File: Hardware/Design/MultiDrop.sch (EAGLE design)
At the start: 12 parts

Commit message: Hardware: evaluation pwr mgt with RPUpi ^1 shield
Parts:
- removed PM2: (no value), Documentation:TRUSTWORTHY
- removed U$5: BUS_MGR, Documentation:BUS_MGR
- added PM1: (no value), Documentation:DESKTOP
- added U$3: BUS_MGR, Documentation:BUS_MGR
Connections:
- net +DTR: now also U$3.+DTR; no longer U$1.+DTR
- net +DTR3: now also U$1.+DTR; no longer U$5.+DTR
- net +RX: now also U$3.+RX; no longer U$1.+RX
- net +RX3: now also U$1.+RX; no longer U$5.+RX
- net +TX: now also U$3.+TX; no longer U$1.+TX
- net +TX3: now also U$1.+TX; no longer U$5.+TX
- net -DTR: now also U$3.-DTR; no longer U$1.-DTR
- net -DTR3: now also U$1.-DTR; no longer U$5.-DTR
- net -RX: now also U$3.-RX; no longer U$1.-RX
- net -RX3: now also U$1.-RX; no longer U$5.-RX
- net -TX: now also U$3.-TX; no longer U$1.-TX
- net -TX3: now also U$1.-TX; no longer U$5.-TX
- net N$1: now also U$3.BM_TX; no longer U$1.BM_TX
- net N$14: now also U$1.BM_TX; no longer U$5.BM_TX
- net N$2: now also U$3.BM_RX; no longer U$1.BM_RX
- net N$21: now also U$1.BM_RX; no longer U$5.BM_RX
- net N$29: now also U$3.PWR; no longer U$1.PWR
- net N$3: now also PM1.TX; no longer PM2.TX
- net N$30: now also BM2.!RESET, U$3.DIO10; no longer BM2.RESET, U$1.DIO
- net N$32: now also U$1.I2C; no longer U$5.I2C
- net N$33: now also U$3.I2C; no longer U$1.I2C
- net N$4: now also U$3.!CTS; no longer U$1.!CTS
- net N$41: now also BM3.SHLD_5V, U$1.PWR; no longer BM3.SHLD_VIN, U$5.PWR
- net N$43: now also BM3.!RESET, U$1.DIO10; no longer BM3.RESET, U$5.DIO
- net N$44: now also BM1.!RESET, U$2.DIO10; no longer BM1.RESET, U$2.DIO
- net N$45: now also BM1.SHLD_5V; no longer BM1.SHLD_VIN
- net N$5: now also U$3.!RTS; no longer U$1.!RTS
- net N$6: now also U$3.!DTR; no longer U$1.!DTR
- net N$7: now also U$3.!DSR; no longer U$1.!DSR
- net N$8: now also U$3.HOST_RX; no longer U$1.PM_RX
- net N$9: now also U$3.HOST_TX; no longer U$1.PM_TX

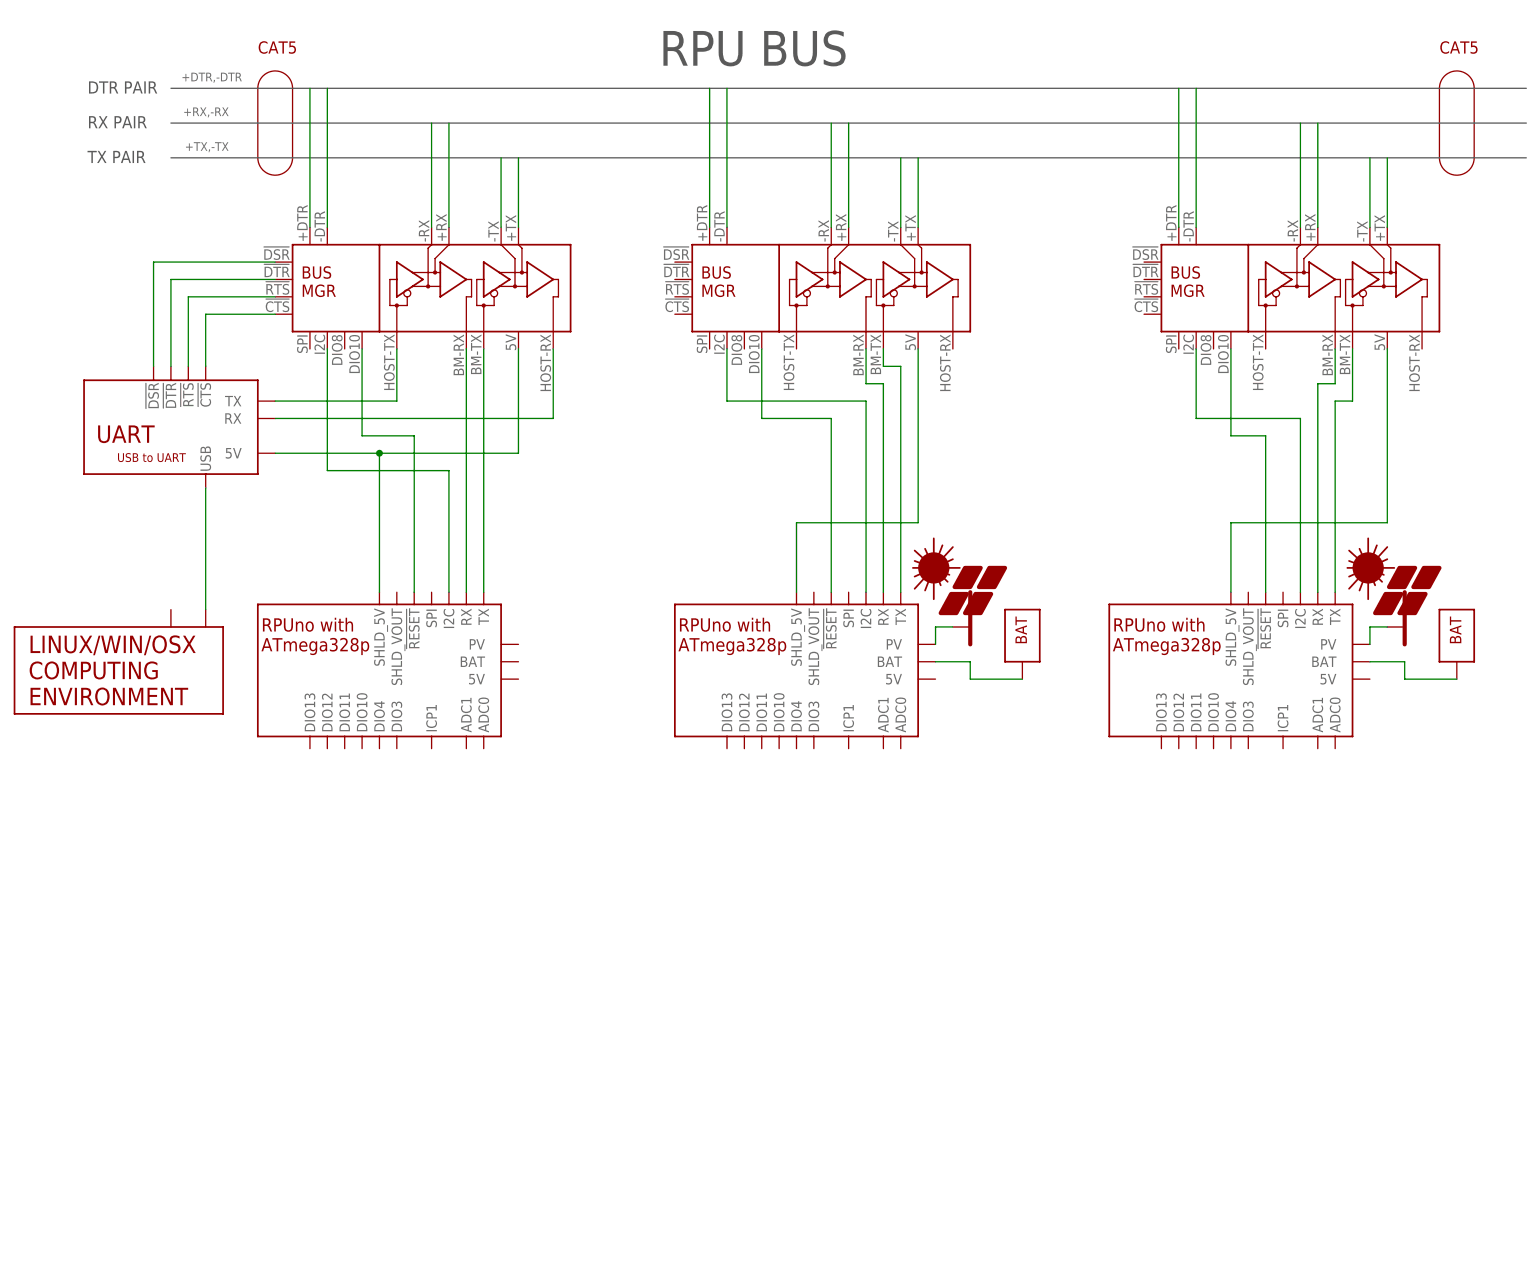
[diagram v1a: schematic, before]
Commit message: Hardware: ^7 review, removed LT3652
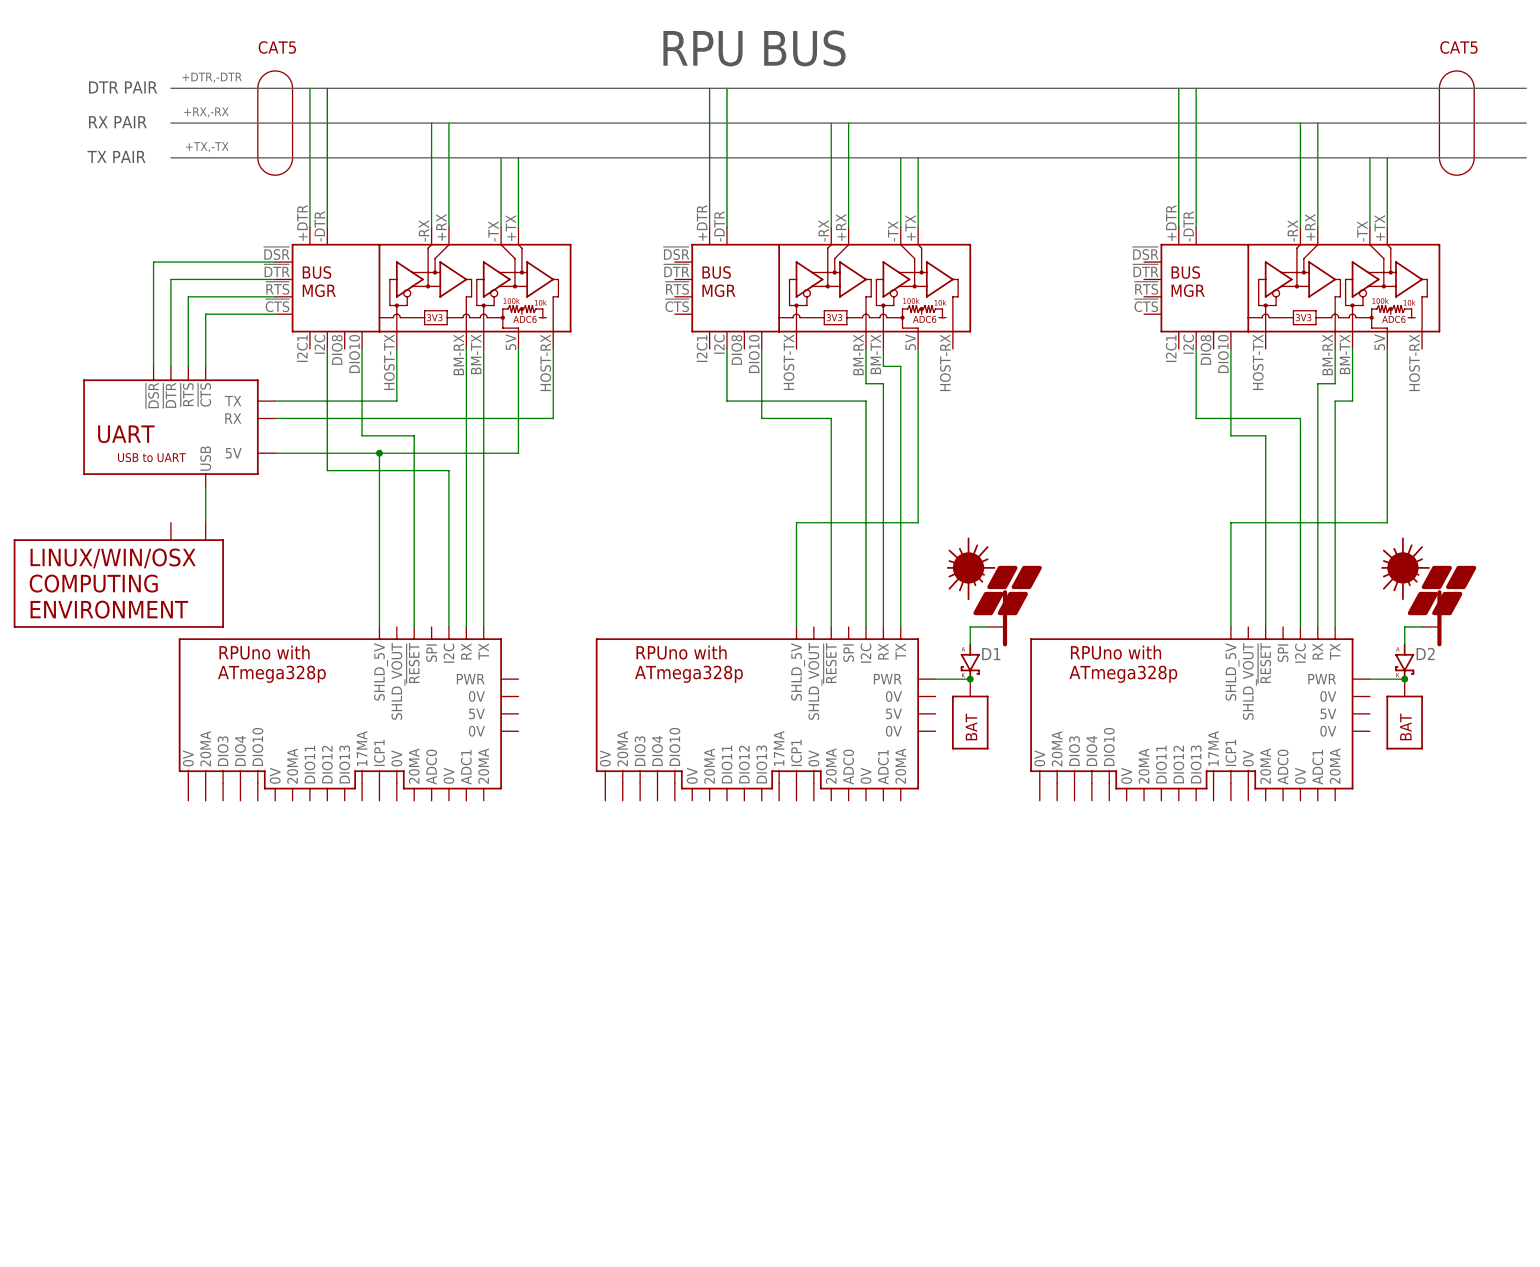
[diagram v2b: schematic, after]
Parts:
- added D1, D2: (no value), D-SBR:DSMC
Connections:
- removed net N$17: BM1.BAT, U$9.BAT_PWR
- removed net N$31: BM3.BAT, U$7.BAT_PWR
- removed net N$34: BM3.PV, PV4.PV_PWR
- removed net N$36: BM1.PV, PV2.PV_PWR
- new net N$12: BM3.PWR, D2.K, U$7.BAT_PWR
- new net N$13: D2.A, PV4.PV_PWR
- new net N$15: BM1.PWR, D1.K, U$9.BAT_PWR
- new net N$16: D1.A, PV2.PV_PWR
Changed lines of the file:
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@@
 <part name="U$3" library="Documentation" deviceset="BUS_MGR" device=""/>
 <part name="PM1" library="Documentation" deviceset="DESKTOP" device=""/>
+<part name="D2" library="D-SBR" deviceset="D" device="SMC"/>
+<part name="D1" library="D-SBR" deviceset="D" device="SMC"/>
 </parts>
 <sheets>
@@
 <instances>
 <instance part="UART1" gate="G$1" x="27.94" y="55.88"/>
-<instance part="PV2" gate="G$1" x="147.32" y="25.4"/>
-<instance part="PV4" gate="G$1" x="210.82" y="25.4"/>
-<instance part="U$7" gate="G$1" x="218.44" y="25.4" rot="R270"/>
-<instance part="U$9" gate="G$1" x="154.94" y="25.4" rot="R270"/>
-<instance part="BM2" gate="G$1" x="60.96" y="20.32"/>
-<instance part="BM1" gate="G$1" x="121.92" y="20.32"/>
-<instance part="BM3" gate="G$1" x="185.42" y="20.32"/>
+<instance part="PV2" gate="G$1" x="152.4" y="25.4"/>
+<instance part="PV4" gate="G$1" x="215.9" y="25.4"/>
+<instance part="U$7" gate="G$1" x="210.82" y="10.16" rot="R90"/>
+<instance part="U$9" gate="G$1" x="147.32" y="10.16" rot="R90"/>
+<instance part="BM2" gate="G$1" x="60.96" y="15.24"/>
+<instance part="BM1" gate="G$1" x="121.92" y="15.24"/>
+<instance part="BM3" gate="G$1" x="185.42" y="15.24"/>
 <instance part="U$1" gate="G$1" x="198.12" y="76.2"/>
 <instance part="U$2" gate="G$1" x="129.54" y="76.2"/>
 <instance part="U$3" gate="G$1" x="71.12" y="76.2"/>
-<instance part="PM1" gate="G$1" x="20.32" y="17.78"/>
+<instance part="PM1" gate="G$1" x="20.32" y="30.48"/>
+<instance part="D2" gate="G$1" x="210.82" y="20.32"/>
+<instance part="D1" gate="G$1" x="147.32" y="20.32"/>
 </instances>
 <busses>
@@
 <net name="N$1" class="0">
 <segment>
-<wire x1="76.2" y1="30.48" x2="76.2" y2="66.04" width="0.1524" layer="91"/>
+<wire x1="76.2" y1="25.4" x2="76.2" y2="66.04" width="0.1524" layer="91"/>
 <pinref part="BM2" gate="G$1" pin="TX"/>
 <pinref part="U$3" gate="G$1" pin="BM_TX"/>
@@
 <net name="N$2" class="0">
 <segment>
-<wire x1="73.66" y1="66.04" x2="73.66" y2="30.48" width="0.1524" layer="91"/>
+<wire x1="73.66" y1="66.04" x2="73.66" y2="25.4" width="0.1524" layer="91"/>
 <pinref part="BM2" gate="G$1" pin="RX"/>
 <pinref part="U$3" gate="G$1" pin="BM_RX"/>
@@
 <net name="N$10" class="0">
 <segment>
-<wire x1="137.16" y1="30.48" x2="137.16" y2="63.5" width="0.1524" layer="91"/>
+<wire x1="137.16" y1="25.4" x2="137.16" y2="63.5" width="0.1524" layer="91"/>
 <wire x1="137.16" y1="63.5" x2="134.62" y2="63.5" width="0.1524" layer="91"/>
 <wire x1="134.62" y1="63.5" x2="134.62" y2="66.04" width="0.1524" layer="91"/>
@@
 <wire x1="132.08" y1="66.04" x2="132.08" y2="60.96" width="0.1524" layer="91"/>
 <wire x1="132.08" y1="60.96" x2="134.62" y2="60.96" width="0.1524" layer="91"/>
-<wire x1="134.62" y1="60.96" x2="134.62" y2="30.48" width="0.1524" layer="91"/>
+<wire x1="134.62" y1="60.96" x2="134.62" y2="25.4" width="0.1524" layer="91"/>
 <pinref part="BM1" gate="G$1" pin="RX"/>
 <pinref part="U$2" gate="G$1" pin="BM_RX"/>
@@
 <net name="N$14" class="0">
 <segment>
-<wire x1="200.66" y1="30.48" x2="200.66" y2="58.42" width="0.1524" layer="91"/>
+<wire x1="200.66" y1="25.4" x2="200.66" y2="58.42" width="0.1524" layer="91"/>
 <wire x1="200.66" y1="58.42" x2="203.2" y2="58.42" width="0.1524" layer="91"/>
 <wire x1="203.2" y1="58.42" x2="203.2" y2="66.04" width="0.1524" layer="91"/>
@@
 <wire x1="200.66" y1="66.04" x2="200.66" y2="60.96" width="0.1524" layer="91"/>
 <wire x1="200.66" y1="60.96" x2="198.12" y2="60.96" width="0.1524" layer="91"/>
-<wire x1="198.12" y1="60.96" x2="198.12" y2="30.48" width="0.1524" layer="91"/>
+<wire x1="198.12" y1="60.96" x2="198.12" y2="25.4" width="0.1524" layer="91"/>
 <pinref part="BM3" gate="G$1" pin="RX"/>
 <pinref part="U$1" gate="G$1" pin="BM_RX"/>
@@
 <net name="N$32" class="0">
 <segment>
-<wire x1="195.58" y1="30.48" x2="195.58" y2="55.88" width="0.1524" layer="91"/>
+<wire x1="195.58" y1="25.4" x2="195.58" y2="55.88" width="0.1524" layer="91"/>
 <wire x1="195.58" y1="55.88" x2="180.34" y2="55.88" width="0.1524" layer="91"/>
 <wire x1="180.34" y1="55.88" x2="180.34" y2="66.04" width="0.1524" layer="91"/>
@@
 </segment>
 </net>
-<net name="N$34" class="0">
-<segment>
-<pinref part="PV4" gate="G$1" pin="PV_PWR"/>
-<wire x1="208.28" y1="25.4" x2="205.74" y2="25.4" width="0.1524" layer="91"/>
-<wire x1="205.74" y1="25.4" x2="205.74" y2="22.86" width="0.1524" layer="91"/>
-<pinref part="BM3" gate="G$1" pin="PV"/>
-</segment>
-</net>
-<net name="N$36" class="0">
-<segment>
-<pinref part="PV2" gate="G$1" pin="PV_PWR"/>
-<wire x1="144.78" y1="25.4" x2="142.24" y2="25.4" width="0.1524" layer="91"/>
-<wire x1="142.24" y1="25.4" x2="142.24" y2="22.86" width="0.1524" layer="91"/>
-<pinref part="BM1" gate="G$1" pin="PV"/>
-</segment>
-</net>
 <net name="N$41" class="0">
 <segment>
@@
 <pinref part="U$1" gate="G$1" pin="PWR"/>
 <pinref part="BM3" gate="G$1" pin="SHLD_5V"/>
-<wire x1="185.42" y1="40.64" x2="185.42" y2="30.48" width="0.1524" layer="91"/>
+<wire x1="185.42" y1="40.64" x2="185.42" y2="25.4" width="0.1524" layer="91"/>
 </segment>
 </net>
 <net name="N$43" class="0">
 <segment>
-<wire x1="190.5" y1="53.34" x2="190.5" y2="30.48" width="0.1524" layer="91"/>
+<wire x1="190.5" y1="53.34" x2="190.5" y2="25.4" width="0.1524" layer="91"/>
 <pinref part="BM3" gate="G$1" pin="!RESET"/>
 <wire x1="190.5" y1="53.34" x2="185.42" y2="53.34" width="0.1524" layer="91"/>
@@
 <wire x1="116.84" y1="66.04" x2="116.84" y2="55.88" width="0.1524" layer="91"/>
 <wire x1="116.84" y1="55.88" x2="127" y2="55.88" width="0.1524" layer="91"/>
-<wire x1="127" y1="55.88" x2="127" y2="30.48" width="0.1524" layer="91"/>
+<wire x1="127" y1="55.88" x2="127" y2="25.4" width="0.1524" layer="91"/>
 <pinref part="BM1" gate="G$1" pin="!RESET"/>
 <pinref part="U$2" gate="G$1" pin="DIO10"/>
@@
 <pinref part="U$2" gate="G$1" pin="PWR"/>
 <pinref part="BM1" gate="G$1" pin="SHLD_5V"/>
-<wire x1="121.92" y1="30.48" x2="121.92" y2="40.64" width="0.1524" layer="91"/>
+<wire x1="121.92" y1="25.4" x2="121.92" y2="40.64" width="0.1524" layer="91"/>
 </segment>
 </net>
@@
 <wire x1="60.96" y1="50.8" x2="81.28" y2="50.8" width="0.1524" layer="91"/>
 <wire x1="81.28" y1="50.8" x2="81.28" y2="66.04" width="0.1524" layer="91"/>
-<wire x1="60.96" y1="30.48" x2="60.96" y2="50.8" width="0.1524" layer="91"/>
+<wire x1="60.96" y1="25.4" x2="60.96" y2="50.8" width="0.1524" layer="91"/>
 <junction x="60.96" y="50.8"/>
 <pinref part="BM2" gate="G$1" pin="SHLD_5V"/>
@@
 <wire x1="58.42" y1="66.04" x2="58.42" y2="53.34" width="0.1524" layer="91"/>
 <wire x1="58.42" y1="53.34" x2="66.04" y2="53.34" width="0.1524" layer="91"/>
-<wire x1="66.04" y1="53.34" x2="66.04" y2="30.48" width="0.1524" layer="91"/>
+<wire x1="66.04" y1="53.34" x2="66.04" y2="25.4" width="0.1524" layer="91"/>
 <pinref part="BM2" gate="G$1" pin="!RESET"/>
 <pinref part="U$3" gate="G$1" pin="DIO10"/>
@@
 <net name="N$33" class="0">
 <segment>
-<wire x1="71.12" y1="30.48" x2="71.12" y2="48.26" width="0.1524" layer="91"/>
+<wire x1="71.12" y1="25.4" x2="71.12" y2="48.26" width="0.1524" layer="91"/>
 <wire x1="71.12" y1="48.26" x2="53.34" y2="48.26" width="0.1524" layer="91"/>
 <wire x1="53.34" y1="48.26" x2="53.34" y2="66.04" width="0.1524" layer="91"/>
@@
 <net name="N$48" class="0">
 <segment>
-<wire x1="132.08" y1="30.48" x2="132.08" y2="58.42" width="0.1524" layer="91"/>
+<wire x1="132.08" y1="25.4" x2="132.08" y2="58.42" width="0.1524" layer="91"/>
 <wire x1="132.08" y1="58.42" x2="111.76" y2="58.42" width="0.1524" layer="91"/>
 <wire x1="111.76" y1="58.42" x2="111.76" y2="66.04" width="0.1524" layer="91"/>
@@
 </segment>
 </net>
-<net name="N$17" class="0">
-<segment>
-<wire x1="142.24" y1="20.32" x2="147.32" y2="20.32" width="0.1524" layer="91"/>
-<wire x1="147.32" y1="20.32" x2="147.32" y2="17.78" width="0.1524" layer="91"/>
+<net name="N$3" class="0">
+<segment>
+<pinref part="UART1" gate="G$1" pin="USB"/>
+<wire x1="35.56" y1="45.72" x2="35.56" y2="40.64" width="0.1524" layer="91"/>
+<pinref part="PM1" gate="G$1" pin="TX"/>
+</segment>
+</net>
+<net name="N$12" class="0">
+<segment>
+<pinref part="U$7" gate="G$1" pin="BAT_PWR"/>
+<pinref part="D2" gate="G$1" pin="K"/>
+<pinref part="BM3" gate="G$1" pin="PWR"/>
+<wire x1="205.74" y1="17.78" x2="210.82" y2="17.78" width="0.1524" layer="91"/>
+<junction x="210.82" y="17.78"/>
+</segment>
+</net>
+<net name="N$13" class="0">
+<segment>
+<pinref part="D2" gate="G$1" pin="A"/>
+<wire x1="210.82" y1="22.86" x2="210.82" y2="25.4" width="0.1524" layer="91"/>
+<wire x1="210.82" y1="25.4" x2="213.36" y2="25.4" width="0.1524" layer="91"/>
+<pinref part="PV4" gate="G$1" pin="PV_PWR"/>
+</segment>
+</net>
+<net name="N$15" class="0">
+<segment>
 <pinref part="U$9" gate="G$1" pin="BAT_PWR"/>
-<wire x1="147.32" y1="17.78" x2="154.94" y2="17.78" width="0.1524" layer="91"/>
-<pinref part="BM1" gate="G$1" pin="BAT"/>
-</segment>
-</net>
-<net name="N$31" class="0">
-<segment>
-<wire x1="205.74" y1="20.32" x2="210.82" y2="20.32" width="0.1524" layer="91"/>
-<wire x1="210.82" y1="20.32" x2="210.82" y2="17.78" width="0.1524" layer="91"/>
-<pinref part="U$7" gate="G$1" pin="BAT_PWR"/>
-<wire x1="210.82" y1="17.78" x2="218.44" y2="17.78" width="0.1524" layer="91"/>
-<pinref part="BM3" gate="G$1" pin="BAT"/>
-</segment>
-</net>
-<net name="N$3" class="0">
-<segment>
-<pinref part="UART1" gate="G$1" pin="USB"/>
-<wire x1="35.56" y1="45.72" x2="35.56" y2="27.94" width="0.1524" layer="91"/>
-<pinref part="PM1" gate="G$1" pin="TX"/>
-</segment>
-</net>
+<pinref part="D1" gate="G$1" pin="K"/>
+<pinref part="BM1" gate="G$1" pin="PWR"/>
+<wire x1="142.24" y1="17.78" x2="147.32" y2="17.78" width="0.1524" layer="91"/>
+<junction x="147.32" y="17.78"/>
+</segment>
+</net>
+<net name="N$16" class="0">
+<segment>
+<pinref part="D1" gate="G$1" pin="A"/>
+<pinref part="PV2" gate="G$1" pin="PV_PWR"/>
+<wire x1="147.32" y1="22.86" x2="147.32" y2="25.4" width="0.1524" layer="91"/>
+<wire x1="147.32" y1="25.4" x2="149.86" y2="25.4" width="0.1524" layer="91"/>
+</segment>
+</net>

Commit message: Hardware: ^8 review
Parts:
- added R1, R2, R3, R4: 50, R-C:R0805
- added SD1, SD2: SD, Documentation:SD
- added U$10, U$11: TT, Documentation:TT
- added U$4, U$5: FT, Documentation:FT
- added U$6, U$8: PT, Documentation:PT
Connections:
- new net N$17: BM1.0V@3, R1.2, R2.1
- new net N$18: BM3.0V@3, R3.2, R4.1
- new net N$19: BM1.20MA@0, U$11.PWR
- new net N$20: BM1.ADC0, R1.1, U$11.4TO20
- new net N$22: BM1.0V@4, U$4.0V
- new net N$23: BM1.ICP1, U$4.OC
- new net N$24: BM1.17MA@0, U$4.PWR
- new net N$25: BM1.ADC1, R2.2, U$6.PWR
- new net N$26: BM1.20MA@1, U$6.4TO20
- new net N$27: BM1.SPI, SD1.PV_PWR
- new net N$28: BM3.SPI, SD2.PV_PWR
- new net N$31: BM3.ADC0, R3.1, U$10.4TO20
- new net N$34: BM3.20MA@0, U$10.PWR
- new net N$35: BM3.0V@4, U$5.0V
- new net N$36: BM3.ICP1, U$5.OC
- new net N$37: BM3.17MA@0, U$5.PWR
- new net N$38: BM3.ADC1, R4.2, U$8.PWR
- new net N$39: BM3.20MA@1, U$8.4TO20
